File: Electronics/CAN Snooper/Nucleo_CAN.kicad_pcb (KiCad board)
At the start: 2 copper layers, 59.1 x 51.4 mm, 39 parts, among them J1 CAN_In, J2 CAN_Out, SW1 Reset, T1 12V Iso Test, T10 CAN L Test, T11 CAN Output GND Test, T2 5V Iso Test, T3 9V Test, T4 3.3V Test, T5 CAN PwrSense Test, T6 CAN Tx Test, T7 CAN Rx Test, T8 CAN Input GND Test, T9 CAN H Test, U1 PDS1-S12-S9-M, U2 MCP1702T-5002E/CB, U3 Nucleo_L432KC, U4 ADM3054

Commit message: CAN Snooper: PCB: Added printing instructions; regenerated previews
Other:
- board text added: "Preview Printing Instructions: * Use "Approx. Scale 1" for accurate sizing * For general fit, use F.Silk, F.Mask, and F.CrtYd * For electrical connections, use F.Cu and B.Cu"
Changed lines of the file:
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@@
     (links 71)
     (no_connects 0)
-    (area 148.689287 47.465 219.280001 104.077381)
+    (area 148.689287 46.83 219.280001 104.077381)
     (thickness 1.6)
-    (drawings 57)
+    (drawings 58)
     (tracks 156)
     (zones 0)
@@
       (net 3 +9V))
   )
+  (gr_text "Preview Printing Instructions:\n* Use \"Approx. Scale 1\" for accurate sizing\n* For general fit, use F.Silk, F.Mask, and F.CrtYd\n* For electrical connections, use F.Cu and B.Cu" (at 158.115 110.49) (layer Cmts.User)
+    (effects (font (size 2.54 2.54) (thickness 0.3)) (justify left))
+  )
   (dimension 51.435 (width 0.3) (layer Dwgs.User)

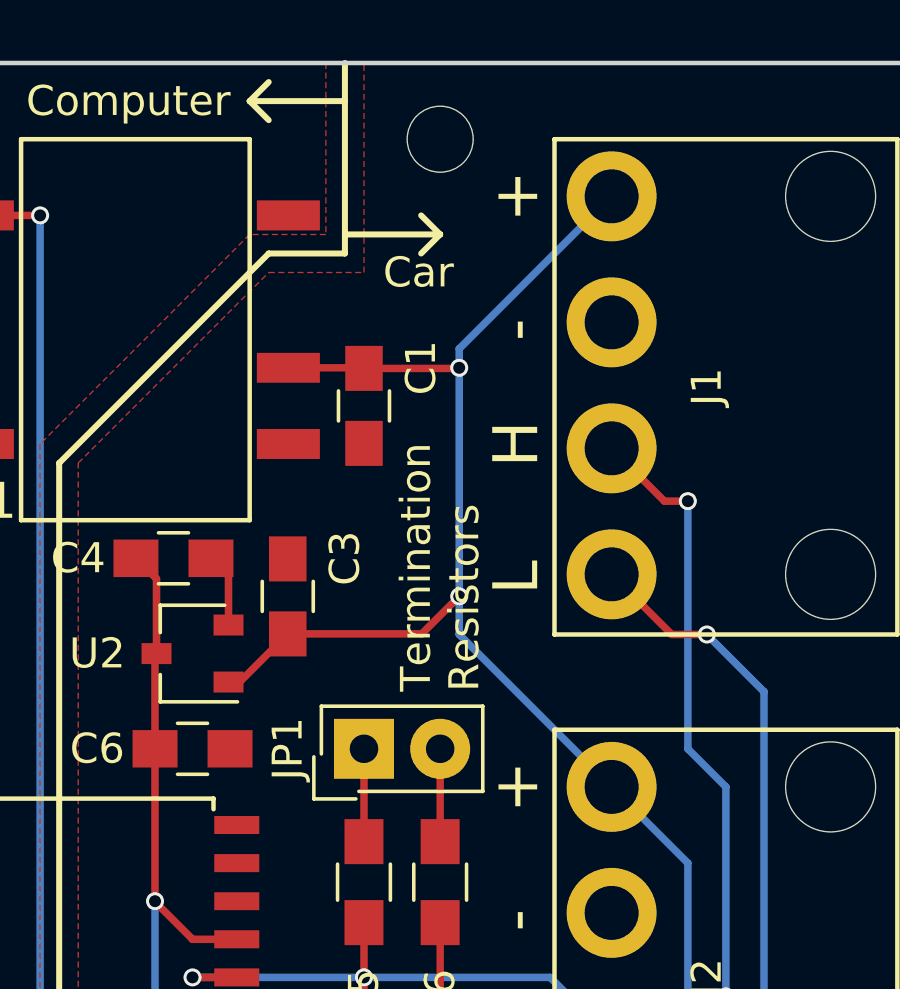
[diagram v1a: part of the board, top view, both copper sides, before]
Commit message: CAN_Snooper: PCB: Increase CAN power trace width to 1.5mm
In order to allow proper power transfer between the two CAN connectors
(that is, along the CAN bus), I increased the trace width of the 12V
line between the connectors and the spoke width on the ground pins of
the connectors. This should allow at least 4A of current without
heating the trace more than 10degC.
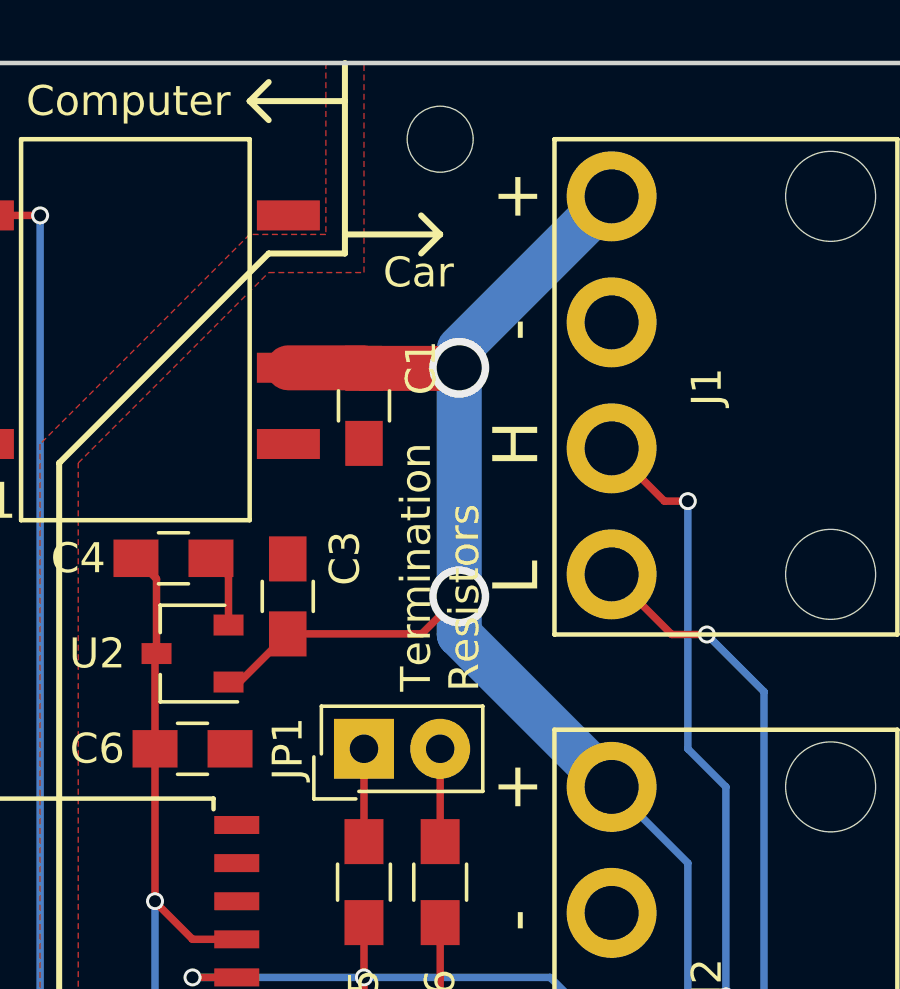
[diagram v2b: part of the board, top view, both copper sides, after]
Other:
- net class Car_Power: clearance 0.2 -> 0.5; trace_width 0.25 -> 1.5; via_dia 0.6 -> 2; via_drill 0.4 -> 1.5
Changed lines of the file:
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@@
     (links 71)
     (no_connects 0)
-    (area 148.689287 46.83 219.280001 104.077381)
+    (area 148.689287 46.83 253.425475 118.837)
     (thickness 1.6)
     (drawings 58)
@@
     (mod_text_size 1 1)
     (mod_text_width 0.15)
-    (pad_size 1.5 0.6)
-    (pad_drill 0)
+    (pad_size 3 3)
+    (pad_drill 1.8)
     (pad_to_mask_clearance 0.2)
     (aux_axis_origin 0 0)
@@
   )
   (net_class Car_Power ""
-    (clearance 0.2)
-    (trace_width 0.25)
-    (via_dia 0.6)
-    (via_drill 0.4)
-    (uvia_dia 0.3)
-    (uvia_drill 0.1)
+    (clearance 0.5)
+    (trace_width 1.5)
+    (via_dia 2)
+    (via_drill 1.5)
+    (uvia_dia 1)
+    (uvia_drill 0.5)
     (add_net +12V)
     (add_net +5VP)
@@
       (net 1 +12V))
     (pad 2 thru_hole circle (at 0 4.2) (size 3 3) (drill 1.8) (layers *.Cu *.Mask)
-      (net 2 GNDPWR))
+      (net 2 GNDPWR) (thermal_width 1))
     (pad 3 thru_hole circle (at 0 8.4) (size 3 3) (drill 1.8) (layers *.Cu *.Mask)
       (net 39 /CAN_H))
@@
       (net 1 +12V))
     (pad 2 thru_hole circle (at 0 4.2) (size 3 3) (drill 1.8) (layers *.Cu *.Mask)
-      (net 2 GNDPWR))
+      (net 2 GNDPWR) (thermal_width 1))
     (pad 3 thru_hole circle (at 0 8.4) (size 3 3) (drill 1.8) (layers *.Cu *.Mask)
       (net 39 /CAN_H))
@@
     (effects (font (size 1.5 1.5) (thickness 0.3)) (justify left))
   )
-  (via (at 200.025 68.58) (size 0.6) (drill 0.4) (layers F.Cu B.Cu) (net 1))
+  (segment (start 200.025 60.325) (end 200.025 60.96) (width 0.25) (layer B.Cu) (net 1))
+  (segment (start 200.025 60.325) (end 205.105 55.245) (width 1.5) (layer B.Cu) (net 1))
+  (segment (start 200.025 68.58) (end 200.025 69.85) (width 1.5) (layer B.Cu) (net 1))
+  (segment (start 205.105 74.93) (end 200.025 69.85) (width 1.5) (layer B.Cu) (net 1))
+  (via (at 200.025 68.58) (size 2) (drill 1.5) (layers F.Cu B.Cu) (net 1))
   (segment (start 194.31 69.83) (end 198.775 69.83) (width 0.25) (layer F.Cu) (net 1))
   (segment (start 198.775 69.83) (end 200.025 68.58) (width 0.25) (layer F.Cu) (net 1))
-  (via (at 200.025 60.96) (size 0.6) (drill 0.4) (layers F.Cu B.Cu) (net 1))
-  (segment (start 196.85 60.98) (end 200.005 60.98) (width 0.25) (layer F.Cu) (net 1))
+  (via (at 200.025 60.96) (size 2) (drill 1.5) (layers F.Cu B.Cu) (net 1))
+  (segment (start 196.85 60.98) (end 200.005 60.98) (width 1.5) (layer F.Cu) (net 1))
   (segment (start 200.005 60.98) (end 200.025 60.96) (width 0.25) (layer F.Cu) (net 1))
-  (segment (start 200.025 60.325) (end 200.025 60.96) (width 0.25) (layer B.Cu) (net 1))
-  (segment (start 200.025 60.325) (end 205.105 55.245) (width 0.25) (layer B.Cu) (net 1))
-  (segment (start 200.025 60.96) (end 200.025 68.58) (width 0.25) (layer B.Cu) (net 1))
-  (segment (start 200.025 68.58) (end 200.025 69.85) (width 0.25) (layer B.Cu) (net 1))
-  (segment (start 205.105 74.93) (end 200.025 69.85) (width 0.25) (layer B.Cu) (net 1))
+  (segment (start 200.025 60.96) (end 200.025 68.58) (width 1.5) (layer B.Cu) (net 1))
   (segment (start 205.105 74.93) (end 207.645 77.47) (width 0.25) (layer B.Cu) (net 1))
   (segment (start 207.01 92.71) (end 207.01 94.615) (width 0.25) (layer F.Cu) (net 1))
@@
   (segment (start 196.87 60.96) (end 196.85 60.98) (width 0.25) (layer F.Cu) (net 1))
   (segment (start 196.85 60.98) (end 196.83 60.96) (width 0.25) (layer F.Cu) (net 1))
-  (segment (start 196.83 60.96) (end 194.33 60.96) (width 0.25) (layer F.Cu) (net 1))
+  (segment (start 196.83 60.96) (end 194.33 60.96) (width 1.5) (layer F.Cu) (net 1))
   (segment (start 194.33 69.85) (end 194.31 69.83) (width 0.25) (layer F.Cu) (net 1) (status 30))
   (segment (start 207.01 97.075) (end 207.01 94.615) (width 0.25) (layer F.Cu) (net 1) (status 10))
